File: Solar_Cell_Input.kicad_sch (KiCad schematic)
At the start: 5 parts, among them J201 Conn_01x04, J202 Conn_01x04, J203 Conn_01x02

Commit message: specified design
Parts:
- removed D201, D202: D, symbol Device:D
- removed J201, J202: Conn_01x04, symbol Connector_Generic:Conn_01x04
- removed J203: Conn_01x02, symbol Connector_Generic:Conn_01x02
- added C301: 1u, Capacitor_SMD:C_0603_1608Metric_Pad1.08x0.95mm_HandSolder, symbol Device:C_Small
- added C302, C303, C304, C305, C306: C_Small, Capacitor_SMD:C_0603_1608Metric_Pad1.08x0.95mm_HandSolder, symbol Device:C_Small
- added D301: D_Schottky, Diode_SMD:D_0805_2012Metric, symbol Device:D_Schottky
- added L301, L302: L_Small, Inductor_SMD:L_Taiyo-Yuden_NR-10050_9.8x10.0mm_HandSoldering, symbol Device:L_Small
- added Q301, Q302: NMOS, Package_TO_SOT_SMD:SOT-23-6, symbol Simulation_SPICE:NMOS
- added Q303: NMOS, Package_TO_SOT_SMD:SOT-23-3, symbol Simulation_SPICE:NMOS
- added R301, R302, R303, R304, R305, R306, R307, R308: TBD, Resistor_SMD:R_0603_1608Metric_Pad0.98x0.95mm_HandSolder, symbol Device:R_Small
- added U301: TMCS1101A2UQDT, Package_SO:SOIC-8_3.9x4.9mm_P1.27mm, symbol Sensor_Current:ACS723xLCTR-40AB
- added U302: TPS61085DGK, Package_SO:VSSOP-8_3x3mm_P0.65mm, symbol Regulator_Switching:TPS61085DGK
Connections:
- net AMEAS: now also U301.7 (VIOUT)
- net GND: now also C301.2, C302.2, C303.2, C304.2, C305.2, C306.2, Q301.1 (D), Q303.1 (D), R303.1, U301.5 (GND), U302.4 (GND)
- new net: R302.1, R303.2, U302.2 (FB)
- new net: C303.1, U302.8 (SS)
- new net: C304.1, R301.1
- new net: R301.2, U302.1 (COMP)
- new net: L301.2, Q301.3 (S), Q302.3 (S)
- new net: Q303.3 (S), R308.1
- new net: D301.2 (A), L302.2, U302.5 (SW)
- new net: Q303.2 (G), R306.1
- new net +5V: C301.1, U301.8 (VCC)
- new net PV_IN: U301.1 (IP+), U301.2 (IP+)
- new net PWM: Q301.2 (G)
- new net Solar_Cell: C302.1, L301.1, L302.1, U301.3 (IP-), U301.4 (IP-), U302.3 (EN), U302.6 (VIN), U302.7 (FREQ)
- new net Switch_SOL_1/EN: R304.1, R305.2
- new net Switch_SOL_1/VIN1: C306.1, Q302.1 (D), R304.2
- new net Switch_SOL_2/EN: R307.1, R308.2
- new net Switch_SOL_2/VIN1: C305.1, D301.1 (K), R302.2, R307.2
- new net TOGGLE: R305.1, R306.2
- new net ~{PWM}: Q302.2 (G)
- no-connect marks 0 -> 5
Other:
- added sheet Switch_SOL_1 (Switch_H.kicad_sch)
- added sheet Switch_SOL_2 (Switch_H.kicad_sch)
- added sheet Temp_sens_solar_cell (Temp_sens.kicad_sch)
- note removed: "Cell Conn"
- note removed: "MPPT"
- note removed: "Temp Sens"
- note removed: "Temp sens Conn"

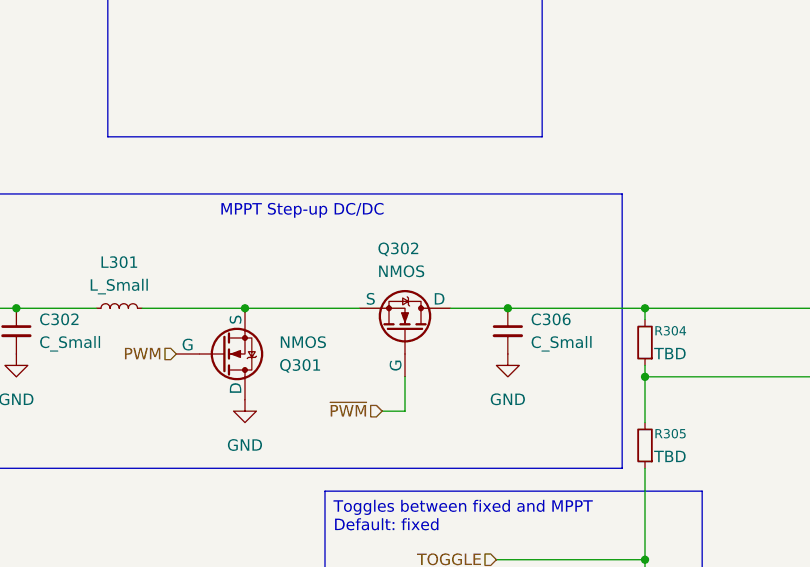
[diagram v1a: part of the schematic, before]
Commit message: added second AMUX and housekeeping
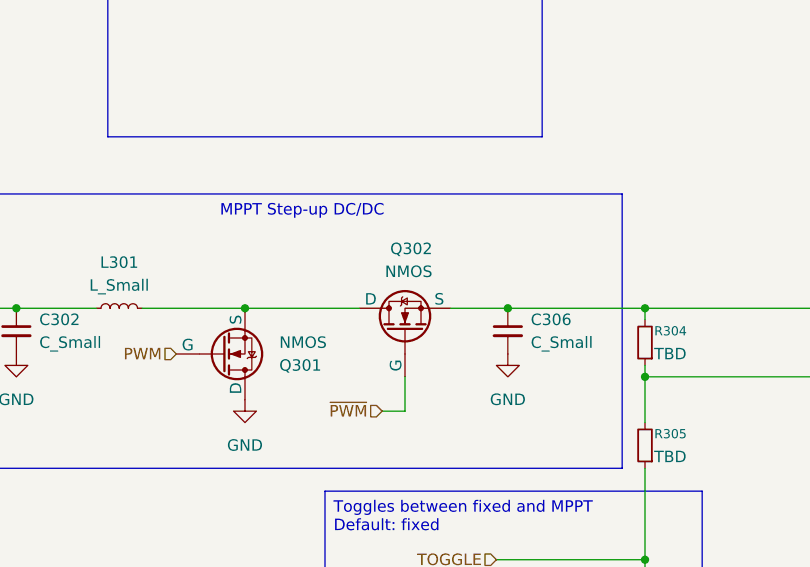
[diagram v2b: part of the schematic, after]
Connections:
- net Switch_SOL_1/VIN1: now also Q302.3 (S); no longer Q302.1 (D)
- net at L301.2, Q301.3 (S): now also Q302.1 (D); no longer Q302.3 (S)
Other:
- moved on the sheet: Q302
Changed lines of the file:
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@@
 	(symbol
 		(lib_id "Simulation_SPICE:NMOS")
-		(at 163.83 74.93 270)
-		(mirror x)
+		(at 163.83 74.93 90)
 		(unit 1)
 		(exclude_from_sim no)
@@
 		(dnp no)
 		(property "Reference" "Q302"
-			(at 160.782 65.786 90)
+			(at 166.878 65.786 90)
 			(effects
 				(font
@@
 		)
 		(property "Value" "NMOS"
-			(at 160.782 68.326 90)
+			(at 166.878 68.326 90)
 			(effects
 				(font
@@
 		)
 		(property "Footprint" "Package_TO_SOT_SMD:SOT-23-6"
-			(at 166.37 69.85 0)
+			(at 161.29 69.85 0)
 			(effects
 				(font
@@
 		)
 		(property "Datasheet" "https://ngspice.sourceforge.io/docs/ngspice-html-manual/manual.xhtml#cha_MOSFETs"
-			(at 151.13 74.93 0)
+			(at 176.53 74.93 0)
 			(effects
 				(font
@@
 		)
 		(property "Sim.Device" "NMOS"
-			(at 146.685 74.93 0)
+			(at 180.975 74.93 0)
 			(effects
 				(font
@@
 		)
 		(property "Sim.Type" "VDMOS"
-			(at 144.78 74.93 0)
+			(at 182.88 74.93 0)
 			(effects
 				(font
@@
 		)
 		(property "Sim.Pins" "1=D 2=G 3=S"
-			(at 148.59 74.93 0)
+			(at 179.07 74.93 0)
 			(effects
 				(font

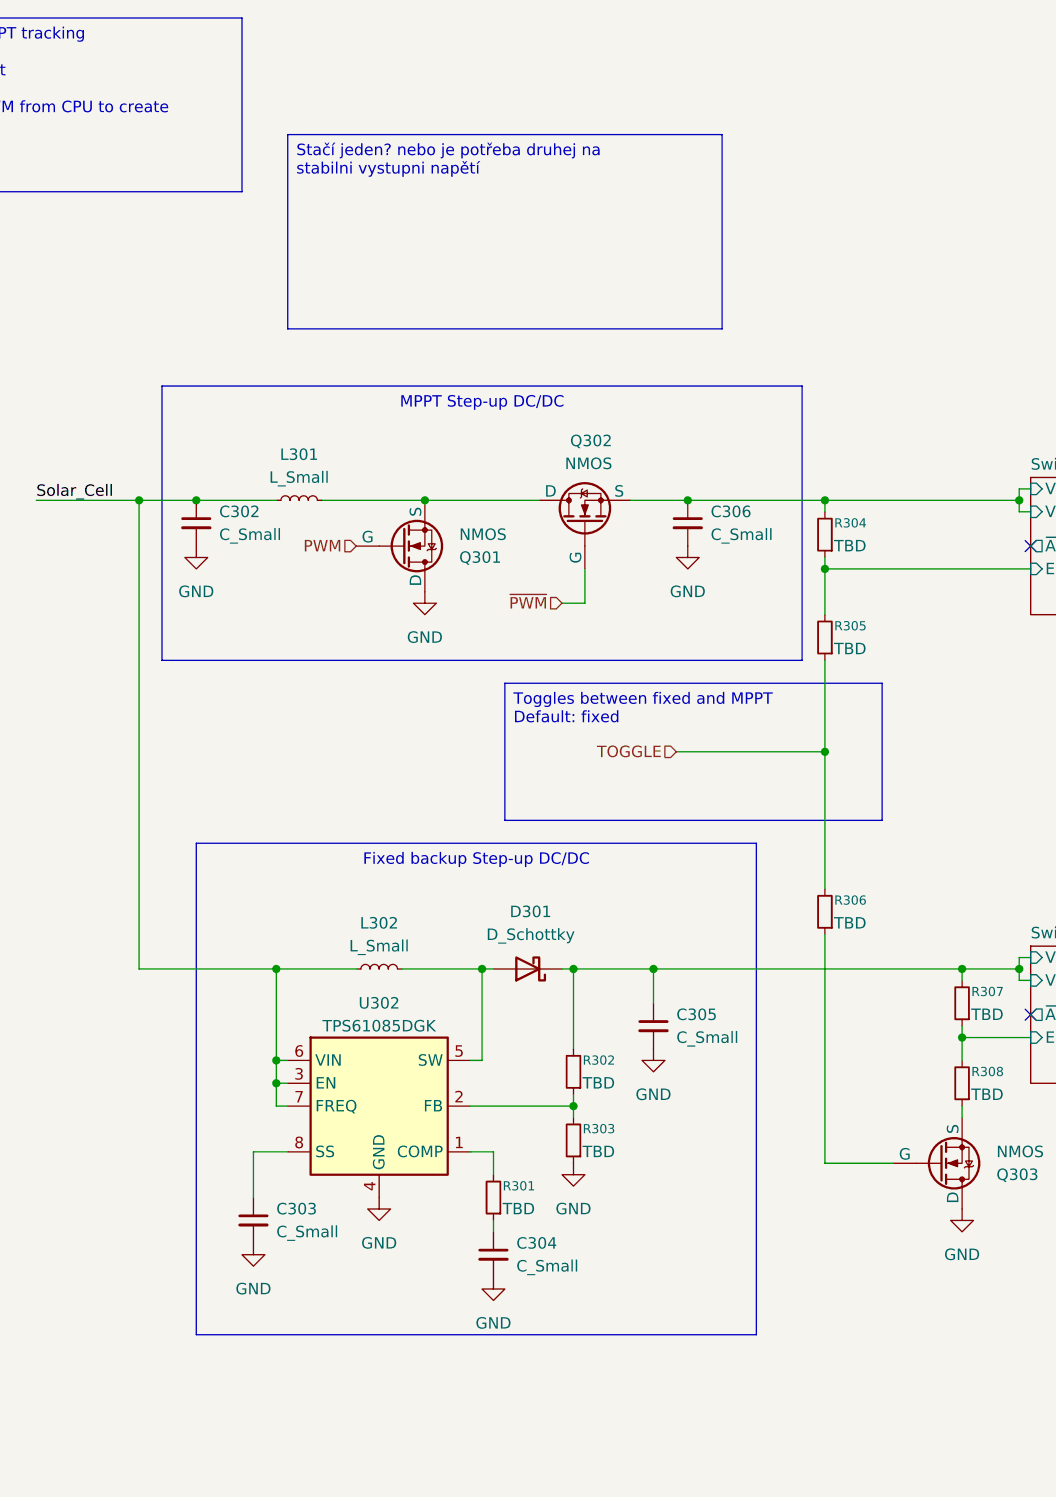
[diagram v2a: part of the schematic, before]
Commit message: connected CAN driver, added 3 solar inputs
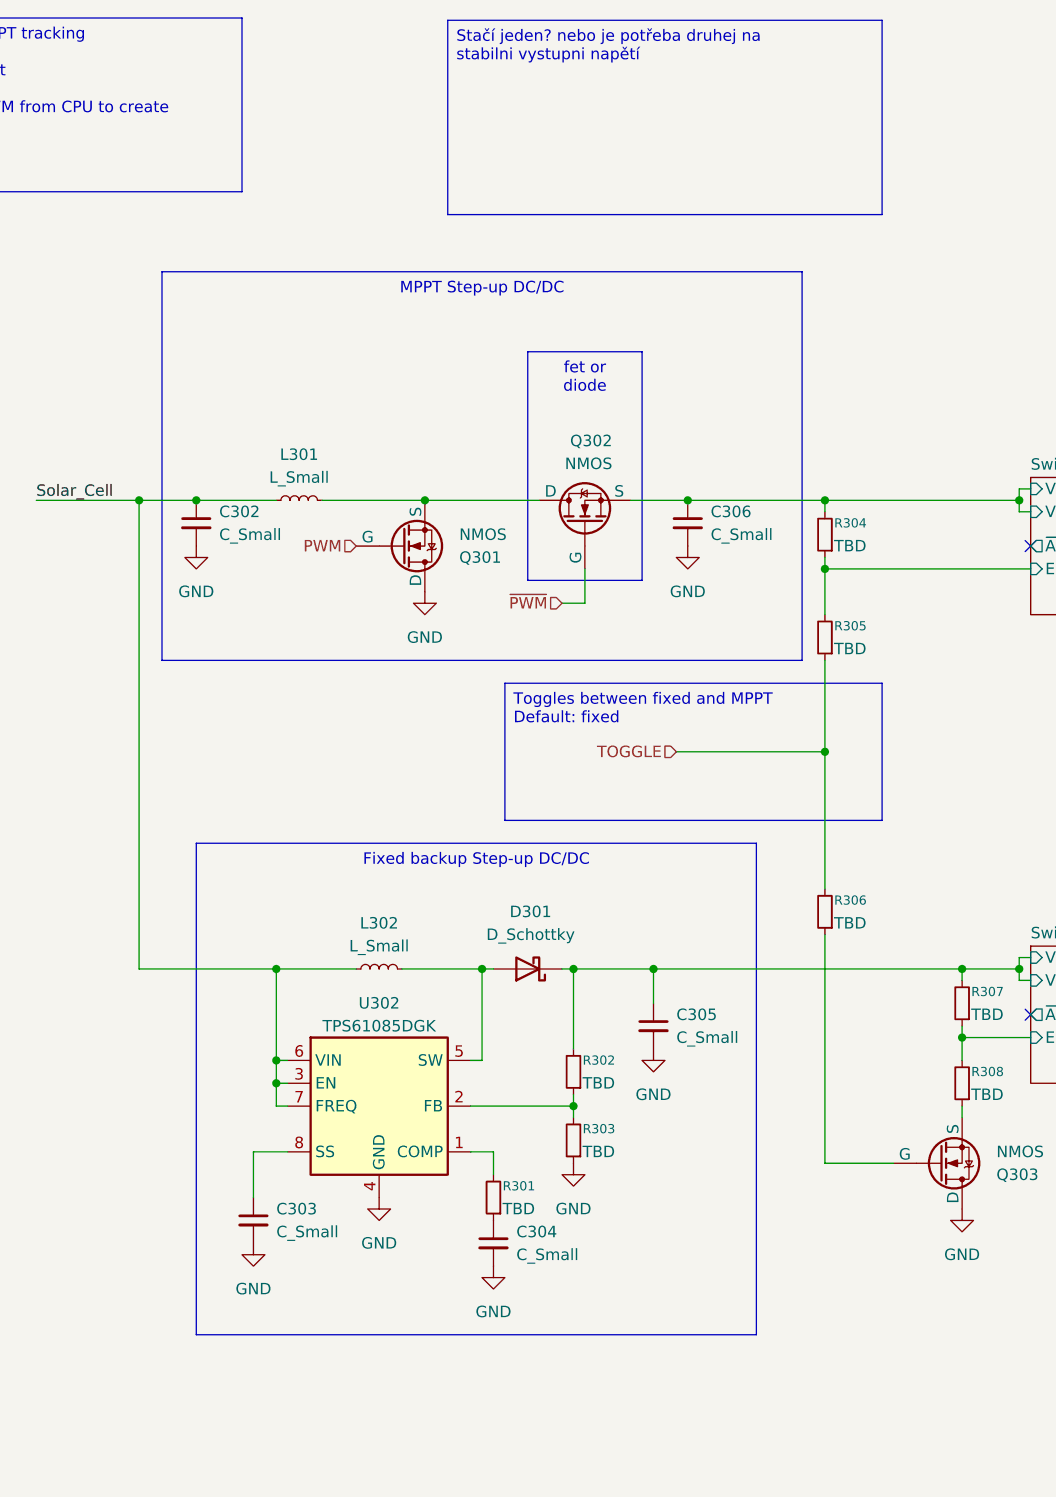
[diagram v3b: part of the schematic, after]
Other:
- moved on the sheet: C304

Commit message: added possible solutions for mppt
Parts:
- removed Q302: NMOS, Package_TO_SOT_SMD:SOT-23-6, symbol Simulation_SPICE:NMOS
- added C201, C202, C203, C204: C_Small, Capacitor_SMD:C_0603_1608Metric_Pad1.08x0.95mm_HandSolder, symbol Device:C_Small
- added D201, D202: D_Schottky, Diode_SMD:D_0805_2012Metric, symbol Device:D_Schottky
- added L201: L_Small, Inductor_SMD:L_Taiyo-Yuden_NR-10050_9.8x10.0mm_HandSoldering, symbol Device:L_Small
- added R201, R202, R203, R204: TBD, Resistor_SMD:R_0603_1608Metric_Pad0.98x0.95mm_HandSolder, symbol Device:R_Small
- added U201: TPS61085DGK, Package_SO:VSSOP-8_3x3mm_P0.65mm, symbol Regulator_Switching:TPS61085DGK
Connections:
- net GND: now also C201.2, C202.2, C203.2, C204.2, U201.4 (GND)
- net PWM: now also R204.2
- net Switch_SOL_1/VIN1: now also D201.1 (K)
- net at L301.2, Q301.3 (S): now also D201.2 (A)
- new net: C201.1, U201.8 (SS)
- new net: C203.1, D202.1 (K), R202.2
- new net: D202.2 (A), L201.2, U201.5 (SW)
- new net: C202.1, R201.1
- new net: C204.1, R203.1, R204.1
- new net: L201.1, U201.3 (EN), U201.6 (VIN), U201.7 (FREQ)
- new net: R201.2, U201.1 (COMP)
- new net: R202.1, R203.2, U201.2 (FB)
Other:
- note added: "LOW PASS; PWM->DC fuguje jako DAC"
- moved on the sheet: Q303, R304, R305, R306, R307, R308

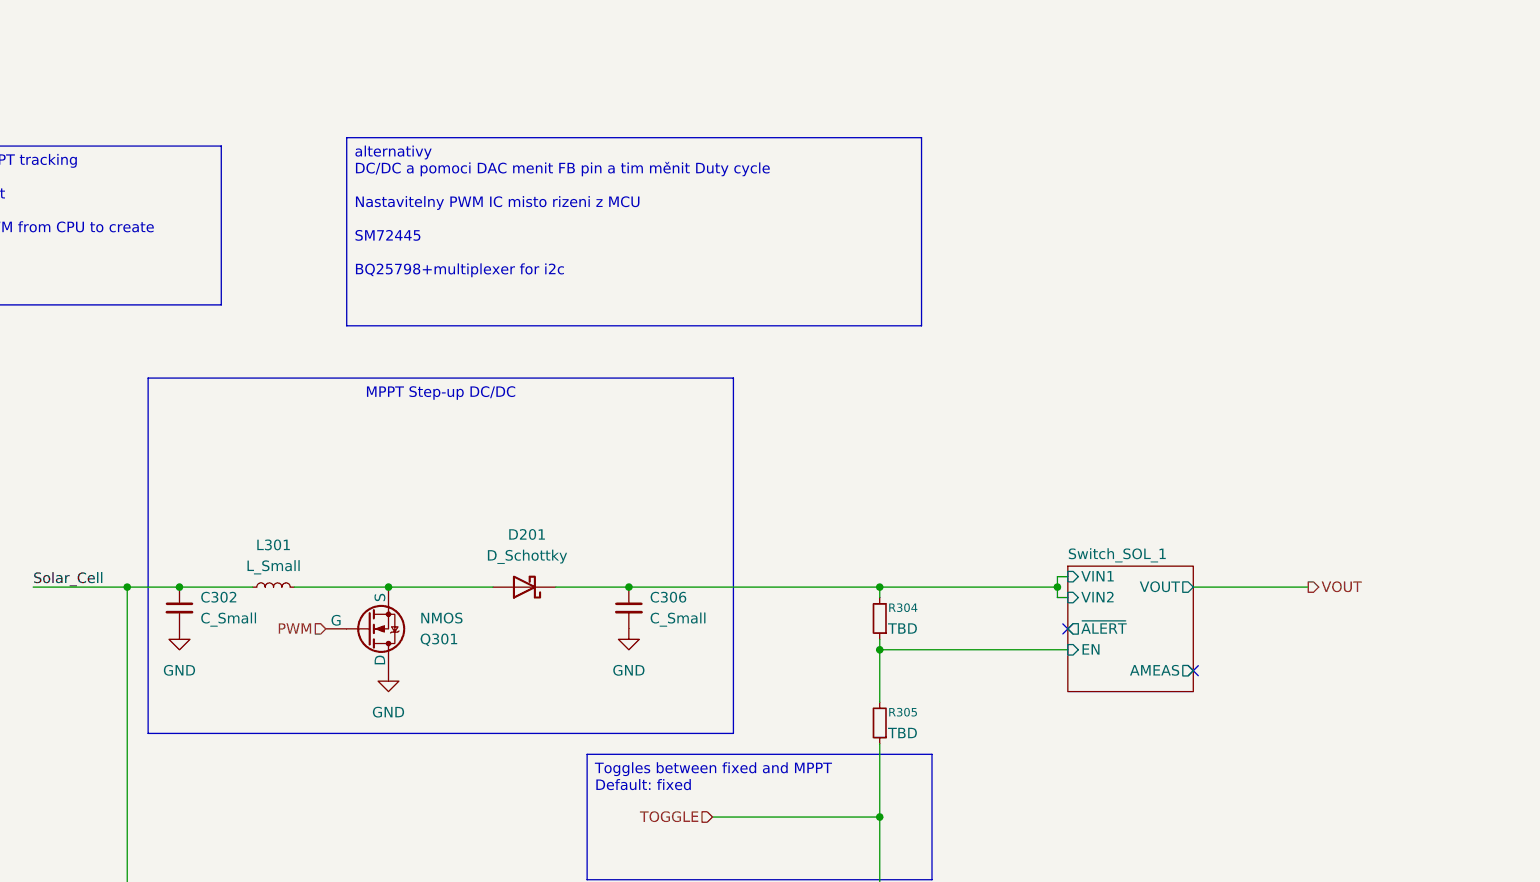
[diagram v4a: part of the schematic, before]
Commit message: changed IO epanders to 2nd MSP430
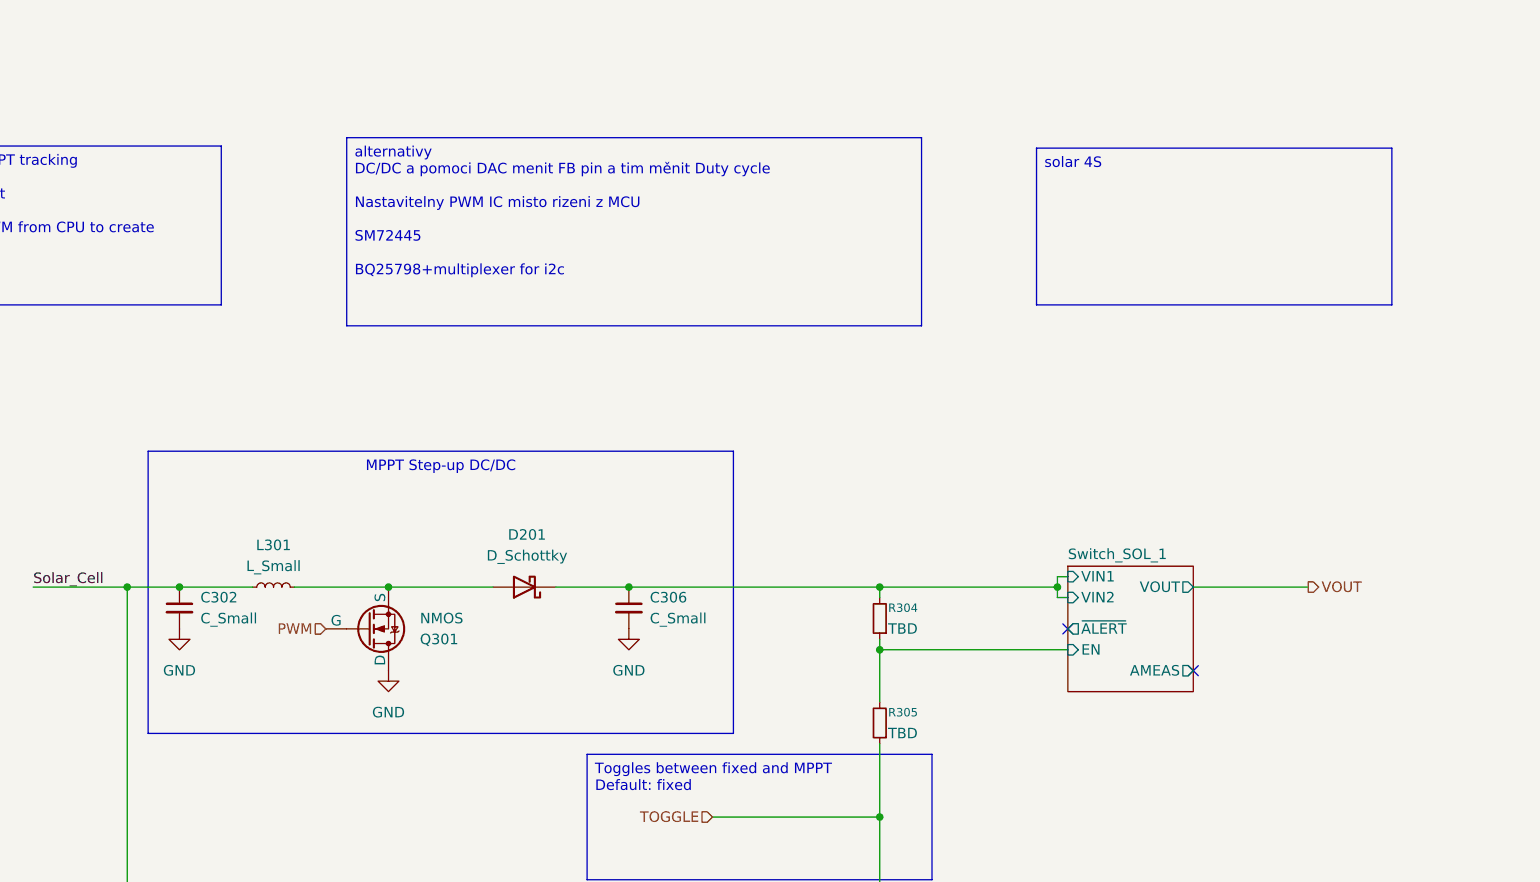
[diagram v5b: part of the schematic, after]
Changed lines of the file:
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@@
+		)
+	)
+	(text_box "solar 4S"
+		(exclude_from_sim no)
+		(at 224.79 19.05 0)
+		(size 43.18 19.05)
+		(margins 0.9525 0.9525 0.9525 0.9525)
+		(stroke
+			(width 0)
+			(type solid)
+		)
+		(fill
+			(type none)
+		)
+		(effects
+			(font
+				(size 1.27 1.27)
+			)
+			(justify left top)
 		)
 	)
@@
 	(text_box "MPPT Step-up DC/DC"
 		(exclude_from_sim no)
-		(at 116.84 46.99 0)
-		(size 71.12 43.18)
+		(at 116.84 55.88 0)
+		(size 71.12 34.29)
 		(margins 0.9525 0.9525 0.9525 0.9525)
 		(stroke

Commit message: added RS422, housekeeping
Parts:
- removed C302, C303, C304, C305, C306: C_Small, Capacitor_SMD:C_0603_1608Metric_Pad1.08x0.95mm_HandSolder, symbol Device:C_Small
- removed D202, D301: D_Schottky, Diode_SMD:D_0805_2012Metric, symbol Device:D_Schottky
- removed L301, L302: L_Small, Inductor_SMD:L_Taiyo-Yuden_NR-10050_9.8x10.0mm_HandSoldering, symbol Device:L_Small
- removed Q301: NMOS, Package_TO_SOT_SMD:SOT-23-6, symbol Simulation_SPICE:NMOS
- removed R301, R302, R303: TBD, Resistor_SMD:R_0603_1608Metric_Pad0.98x0.95mm_HandSolder, symbol Device:R_Small
- removed U201, U302: TPS61085DGK, Package_SO:VSSOP-8_3x3mm_P0.65mm, symbol Regulator_Switching:TPS61085DGK
- added C205, C206, C207, C208: 1u, Capacitor_SMD:C_0603_1608Metric_Pad1.08x0.95mm_HandSolder, symbol Device:C_Small
- added Q201, Q202, Q203: NMOS, Package_TO_SOT_SMD:SOT-23-3, symbol Simulation_SPICE:NMOS
- added R205, R206, R207, R208: R_Small, Resistor_SMD:R_0603_1608Metric_Pad0.98x0.95mm_HandSolder, symbol Device:R_Small
- added U201: BQ24650, Package_DFN_QFN:Texas_RVA_VQFN-16-1EP_3.5x3.5mm_P0.5mm_EP2.14x2.14mm_ThermalVias, symbol Battery_Management:BQ24650
- C201, C202, C203, C204: value C_Small -> 1u
- R201, R202, R203, R204: value TBD -> R_Small
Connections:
- net GND: now also R203.2, C206.2, C207.2, Q201.3 (S), Q203.3 (S), R207.2, R208.2, U201.11 (GND), U201.17 (GND); no longer C202.2
- net Solar_Cell: no longer U301.3 (IP-), U301.4 (IP-)
- net Switch_SOL_1/VIN1: now also R202.1, R204.1, C205.2, C206.1, C207.1, C208.1, U201.9 (SRN); no longer D201.1 (K)
- net at C201.1: now also R201.1, U201.1 (VCC)
- net at R202.2: now also L201.2, C205.1, U201.10 (SRP); no longer C203.1
- net at C202.1: now also L201.1, Q201.1 (D), Q202.3 (S), U201.14 (PH); no longer R201.1
- net REGN: now reaches D201.2 (A)
- net REGN: now also C203.1, U201.12 (REGN)
- net PV: now reaches R201.2
- net PV: now also C204.1, U301.3 (IP-), U301.4 (IP-), Q202.1 (D), R205.1
- net PWM: no longer names the net of R204.2
- net PWM: now also R203.1, C208.2, U201.8 (VFB)
- net Switch_SOL_2/VIN1 renamed 5V_DCDC_1/VOUT
- new net: C202.2, D201.1 (K), U201.16 (BTST)
- new net: R206.1, U201.6 (VREF), U201.7 (TERM_EN)
- new net: Q203.1 (D), R205.2, R208.1, U201.2 (MPPSET)
- new net: Q202.2 (G), U201.15 (HIDRV)
- new net: Q201.2 (G), U201.13 (LODRV)
- new net Term: R206.2, R207.1, U201.4 (TS)
- new net ~{CE}: Q203.2 (G)
- no-connect marks 5 -> 7
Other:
- added sheet 5V_DCDC_1 (LDO_5V.kicad_sch)
- note removed: "LOW PASS; PWM->DC fuguje jako DAC"
- moved on the sheet: C301, Q303, R304, R305, R306, R307, R308, U301
